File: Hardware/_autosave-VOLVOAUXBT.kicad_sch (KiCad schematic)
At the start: 81 parts, among them J1 10118193-0001LF, J10 Conn_01x02_Pin, J11 Conn_01x02_Pin, J12 Conn_01x05_Pin, J13 Conn_01x05_Pin, J14 Conn_01x05_Pin, J15 Conn_01x02_Pin, J16 Conn_01x02_Pin, J17 Conn_01x01_Pin, J18 Conn_01x02_Pin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

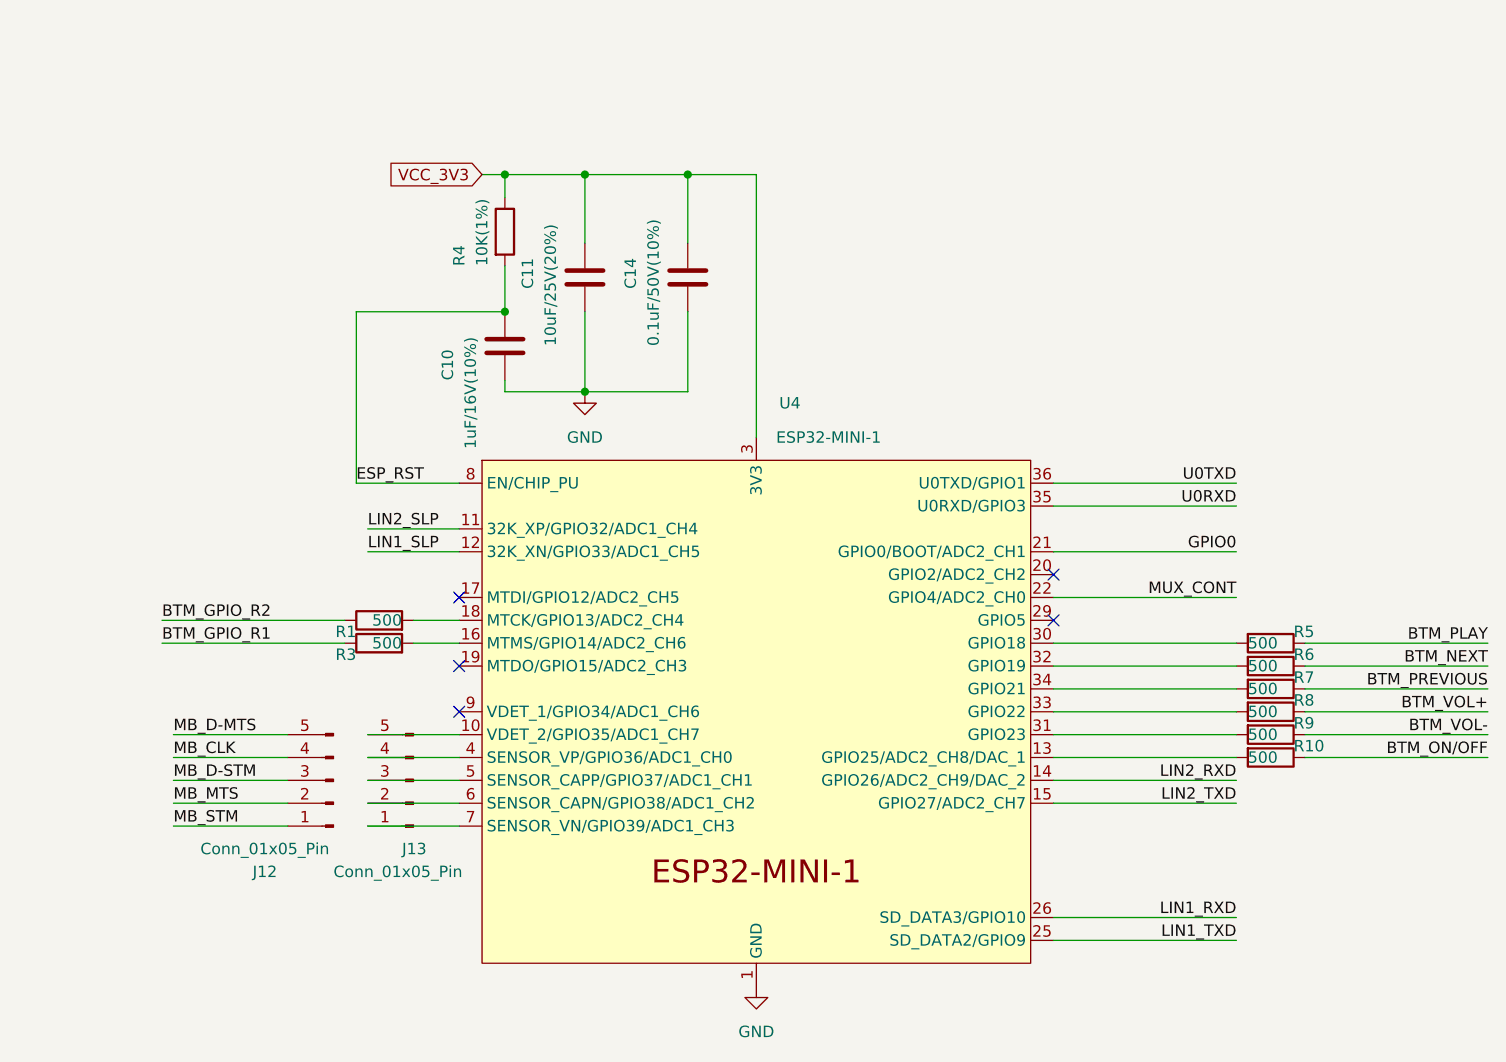
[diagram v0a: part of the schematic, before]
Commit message: Swap to ESP32-wroom-32e. Updated PCB too
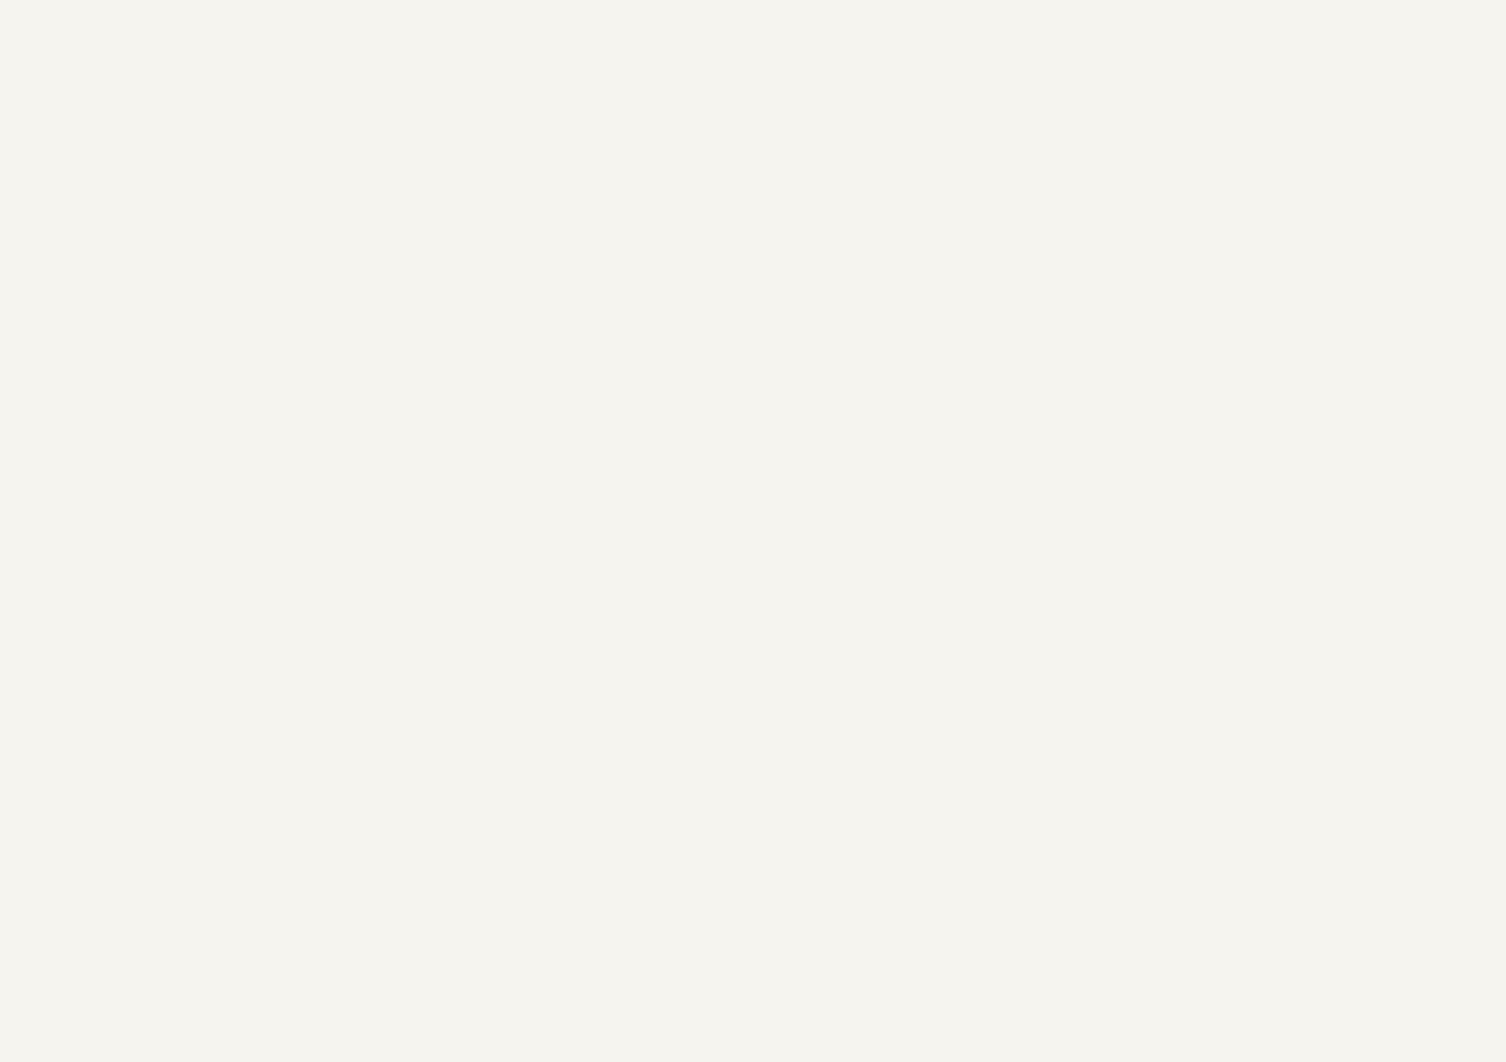
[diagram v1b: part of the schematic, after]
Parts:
- removed C10: 1uF/16V(10%), Capacitor_SMD:C_1206_3216Metric, symbol Device:C
- removed C11: 10uF/25V(20%), Capacitor_SMD:C_1206_3216Metric, symbol Device:C
- removed C14: 0.1uF/50V(10%), Capacitor_SMD:C_1206_3216Metric, symbol Device:C
- removed J12, J13: Conn_01x05_Pin, Connector_PinHeader_2.54mm:PinHeader_1x05_P2.54mm_Vertical, symbol Connector:Conn_01x05_Pin
- removed R1, R10, R3, R5, R6, R7, R8, R9: 500, Resistor_SMD:R_0603_1608Metric, symbol Device:R
- removed R4: 10K(1%), Resistor_SMD:R_0603_1608Metric, symbol Device:R
- removed U4: ESP32-MINI-1, PCM_Espressif:ESP32-MINI-1, symbol PCM_Espressif:ESP32-MINI-1
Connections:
- no-connect marks 42 -> 37
